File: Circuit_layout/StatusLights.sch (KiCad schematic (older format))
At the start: 34 parts, among them Q1 ZVP4525G, U1 PDM2-S24-S12, U11 TLP293, U12 TLP293, U16 LTC3638, U27 TLP293

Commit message: Completed errata changes
Committing before annotation, footprint assignment, and board relayout for backup purposes
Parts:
- removed C19: 10uF, Capacitors_SMD:C_0805_HandSoldering, symbol C
- removed C3: 2.2uF, Capacitors_SMD:C_0805_HandSoldering, symbol C
- removed D5: D_Schottky, custom_footprints:do214ac, symbol D_Schottky
- removed L1: 100uH, Inductors:Inductor_Taiyo-Yuden_NR-80xx_HandSoldering, symbol INDUCTOR
- removed R16, R19, R20, R69: 250k, Resistors_SMD:R_0805_HandSoldering, symbol R
- removed R70: 47k, Resistors_SMD:R_0805_HandSoldering, symbol R
- removed R76: 750k, Resistors_SMD:R_0805_HandSoldering, symbol R
- removed R77: 196k, Resistors_SMD:R_0805_HandSoldering, symbol R
- removed U1: PDM2-S24-S12, custom_footprints:DCDC-Conv_TRACO_TMR_1-xxxx_Single, symbol PDM2-S24-S12-RESCUE-Circuit_layout
- removed U16: LTC3638, custom_footprints:TSSOP16_LTC3638, symbol LTC3638
- added R?: 4.3K, symbol R
- added R?: 250k, symbol R
- added U?: RUW15SL12C, symbol RUW15SL12C
- C?: renamed from C24; value 1uF -> 10uF
- D1, D2, D3, D4: symbol LED -> LED-RESCUE-Circuit_layout
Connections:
- net GND: now also U?.8 (-Vout)
- net HV+: now also HVPL_HV1.1, R?.2, U?.5 (+Vin)
- net HV-: now also R?.2, U?.4 (-Vin)
- net HVPL: now also U?.7 (+Vout)
- new net: R?.1, R?.1, U?.1 (ON/OFF)
- no-connect marks 1 -> 3
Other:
- moved on the sheet: C?, GLV_GND1, HVPL_HV1, HVPL_LV1, HV_GND1

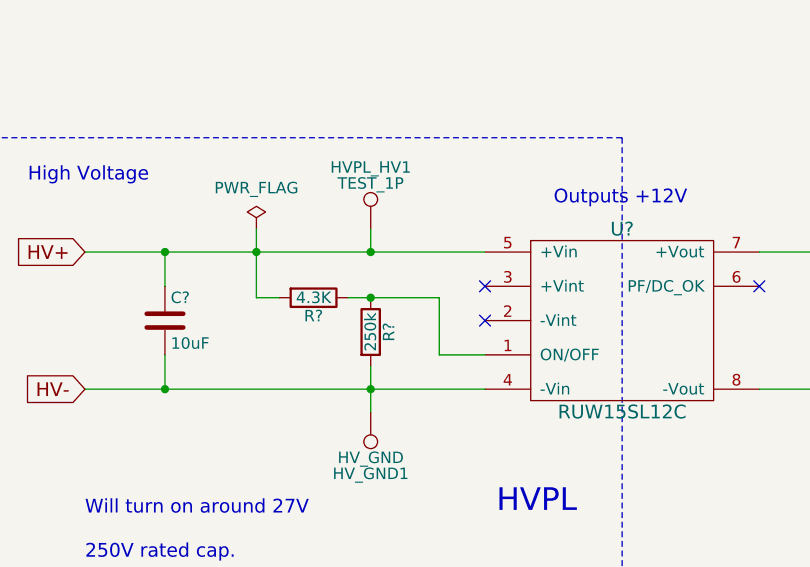
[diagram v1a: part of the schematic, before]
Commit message: Associated footprints and generated new netlist
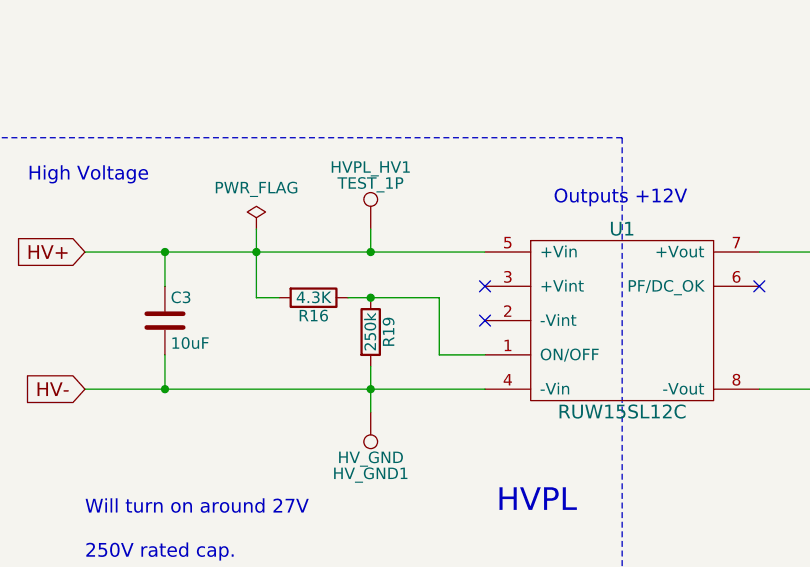
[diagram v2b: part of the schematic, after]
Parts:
- C3: renamed from C?; footprint Capacitors_SMD:C_2220_HandSoldering -> Capacitors_THT:CP_Radial_D10.0mm_P5.00mm
- R16, R19: renamed from R?; footprint (none) -> Resistors_SMD:R_0805_HandSoldering
- U1: renamed from U?; footprint (none) -> custom_footprints:RUW15
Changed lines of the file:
@@
 $EndComp
 $Comp
-L C C?
+L C C3
 U 1 1 58C1AF35
 P 1200 5600
-F 0 "C?" H 1225 5700 50  0000 L CNN
+F 0 "C3" H 1225 5700 50  0000 L CNN
 F 1 "10uF" H 1225 5500 50  0000 L CNN
-F 2 "Capacitors_SMD:C_2220_HandSoldering" H 1238 5450 50  0001 C CNN
+F 2 "Capacitors_THT:CP_Radial_D10.0mm_P5.00mm" H 1238 5450 50  0001 C CNN
 F 3 "" H 1200 5600 50  0000 C CNN
 F 4 "490-3550-1-ND" H 1200 5600 60  0001 C CNN "DigiKey P/N"
@@
 NoConn ~ 2600 5450
 $Comp
-L RUW15SL12C U?
+L RUW15SL12C U1
 U 1 1 5A7E5026
 P 3200 5600
-F 0 "U?" H 3200 6000 60  0000 C CNN
+F 0 "U1" H 3200 6000 60  0000 C CNN
 F 1 "RUW15SL12C" H 3200 5200 60  0000 C CNN
-F 2 "" H 2850 6000 60  0001 C CNN
+F 2 "custom_footprints:RUW15" H 2850 6000 60  0001 C CNN
 F 3 "" H 2850 6000 60  0001 C CNN
 	1    3200 5600
@@
 NoConn ~ 3800 5450
 $Comp
-L R R?
+L R R16
 U 1 1 5A7E9A17
 P 1850 5500
-F 0 "R?" V 1930 5500 50  0000 C CNN
+F 0 "R16" V 1930 5500 50  0000 C CNN
 F 1 "4.3K" V 1850 5500 50  0000 C CNN
-F 2 "" V 1780 5500 50  0000 C CNN
+F 2 "Resistors_SMD:R_0805_HandSoldering" V 1780 5500 50  0001 C CNN
 F 3 "" H 1850 5500 50  0000 C CNN
 	1    1850 5500
@@
 $EndComp
 $Comp
-L R R?
+L R R19
 U 1 1 5A7E9ABB
 P 2100 5650
-F 0 "R?" V 2180 5650 50  0000 C CNN
+F 0 "R19" V 2180 5650 50  0000 C CNN
 F 1 "250k" V 2100 5650 50  0000 C CNN
-F 2 "" V 2030 5650 50  0000 C CNN
+F 2 "Resistors_SMD:R_0805_HandSoldering" V 2030 5650 50  0001 C CNN
 F 3 "" H 2100 5650 50  0000 C CNN
 	1    2100 5650

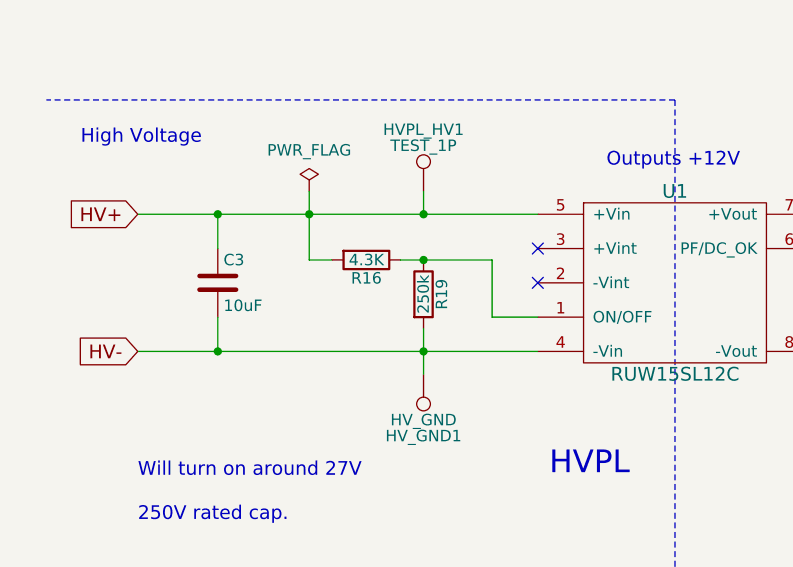
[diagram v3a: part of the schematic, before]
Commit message: Wider traces for DC/DC converter
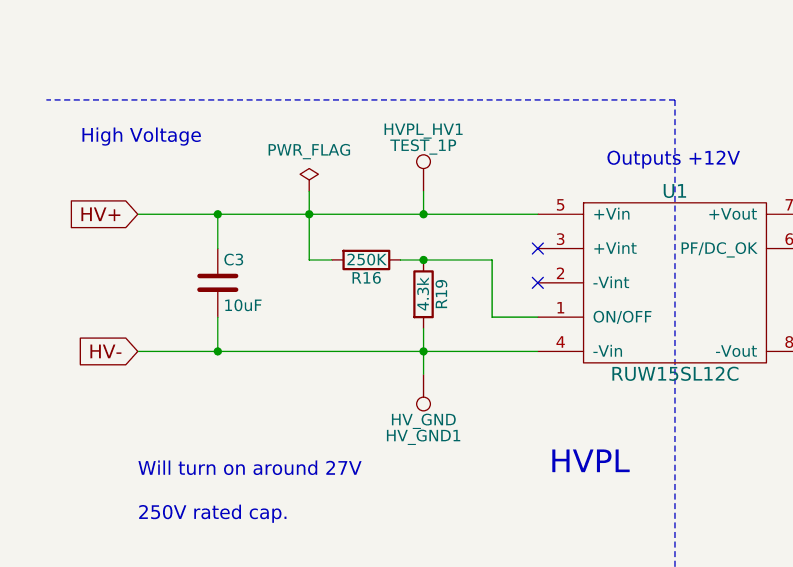
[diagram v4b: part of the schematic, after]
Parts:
- R16: value 4.3K -> 250K
- R19: value 250k -> 4.3k
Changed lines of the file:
@@
 P 1850 5500
 F 0 "R16" V 1930 5500 50  0000 C CNN
-F 1 "4.3K" V 1850 5500 50  0000 C CNN
+F 1 "250K" V 1850 5500 50  0000 C CNN
 F 2 "Resistors_SMD:R_0805_HandSoldering" V 1780 5500 50  0001 C CNN
 F 3 "" H 1850 5500 50  0000 C CNN
@@
 P 2100 5650
 F 0 "R19" V 2180 5650 50  0000 C CNN
-F 1 "250k" V 2100 5650 50  0000 C CNN
+F 1 "4.3k" V 2100 5650 50  0000 C CNN
 F 2 "Resistors_SMD:R_0805_HandSoldering" V 2030 5650 50  0001 C CNN
 F 3 "" H 2100 5650 50  0000 C CNN

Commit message: Generated gerber and drill files for board ordering
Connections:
- net CC_LED renamed SPARE_LED
- net CC_LED_CTRL renamed SPARE_LED_CTRL
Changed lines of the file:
@@
 $EndComp
 $Comp
-L GND #PWR038
+L GND #PWR043
 U 1 1 58AF33D9
 P 4250 1300
-F 0 "#PWR038" H 4250 1050 50  0001 C CNN
+F 0 "#PWR043" H 4250 1050 50  0001 C CNN
 F 1 "GND" H 4250 1150 50  0000 C CNN
 F 2 "" H 4250 1300 50  0000 C CNN
@@
 $EndComp
 $Comp
-L +24V #PWR039
+L +24V #PWR044
 U 1 1 58AF3526
 P 5650 850
-F 0 "#PWR039" H 5650 700 50  0001 C CNN
+F 0 "#PWR044" H 5650 700 50  0001 C CNN
 F 1 "+24V" H 5650 990 50  0000 C CNN
 F 2 "" H 5650 850 50  0000 C CNN
@@
 $EndComp
 $Comp
-L GND #PWR040
+L GND #PWR045
 U 1 1 58AF4273
 P 4250 2500
-F 0 "#PWR040" H 4250 2250 50  0001 C CNN
+F 0 "#PWR045" H 4250 2250 50  0001 C CNN
 F 1 "GND" H 4250 2350 50  0000 C CNN
 F 2 "" H 4250 2500 50  0000 C CNN
@@
 $EndComp
 $Comp
-L +24V #PWR041
+L +24V #PWR046
 U 1 1 58AF427B
 P 5650 2000
-F 0 "#PWR041" H 5650 1850 50  0001 C CNN
+F 0 "#PWR046" H 5650 1850 50  0001 C CNN
 F 1 "+24V" H 5650 2140 50  0000 C CNN
 F 2 "" H 5650 2000 50  0000 C CNN
@@
 $EndComp
 $Comp
-L GND #PWR042
+L GND #PWR047
 U 1 1 58B26825
 P 8750 1200
-F 0 "#PWR042" H 8750 950 50  0001 C CNN
+F 0 "#PWR047" H 8750 950 50  0001 C CNN
 F 1 "GND" H 8750 1050 50  0000 C CNN
 F 2 "" H 8750 1200 50  0000 C CNN
@@
 $EndComp
 $Comp
-L GND #PWR043
+L GND #PWR048
 U 1 1 58B26F4E
 P 8750 1650
-F 0 "#PWR043" H 8750 1400 50  0001 C CNN
+F 0 "#PWR048" H 8750 1400 50  0001 C CNN
 F 1 "GND" H 8750 1500 50  0000 C CNN
 F 2 "" H 8750 1650 50  0000 C CNN
@@
 $EndComp
 $Comp
-L GND #PWR044
+L GND #PWR049
 U 1 1 58B272AA
 P 8750 2100
-F 0 "#PWR044" H 8750 1850 50  0001 C CNN
+F 0 "#PWR049" H 8750 1850 50  0001 C CNN
 F 1 "GND" H 8750 1950 50  0000 C CNN
 F 2 "" H 8750 2100 50  0000 C CNN
@@
 $EndComp
 $Comp
-L GND #PWR045
+L GND #PWR050
 U 1 1 58B27330
 P 8750 2550
-F 0 "#PWR045" H 8750 2300 50  0001 C CNN
+F 0 "#PWR050" H 8750 2300 50  0001 C CNN
 F 1 "GND" H 8750 2400 50  0000 C CNN
 F 2 "" H 8750 2550 50  0000 C CNN
@@
 Blue
 $Comp
-L +5V #PWR046
+L +5V #PWR051
 U 1 1 58B2809B
 P 10250 1100
-F 0 "#PWR046" H 10250 950 50  0001 C CNN
+F 0 "#PWR051" H 10250 950 50  0001 C CNN
 F 1 "+5V" H 10250 1240 50  0000 C CNN
 F 2 "" H 10250 1100 50  0000 C CNN
@@
 	4800 4500 4950 4500
 $Comp
-L +24V #PWR047
+L +24V #PWR052
 U 1 1 58C523A5
 P 4800 3700
-F 0 "#PWR047" H 4800 3550 50  0001 C CNN
+F 0 "#PWR052" H 4800 3550 50  0001 C CNN
 F 1 "+24V" H 4800 3840 50  0000 C CNN
 F 2 "" H 4800 3700 50  0000 C CNN
@@
 $EndComp
 $Comp
-L PWR_FLAG #FLG048
+L PWR_FLAG #FLG053
 U 1 1 58C1AF3D
 P 1600 5200
-F 0 "#FLG048" H 1600 5295 50  0001 C CNN
+F 0 "#FLG053" H 1600 5295 50  0001 C CNN
 F 1 "PWR_FLAG" H 1600 5380 50  0000 C CNN
 F 2 "" H 1600 5200 50  0000 C CNN
@@
 	1250 1600 1400 1600
 $Comp
-L GND #PWR049
+L GND #PWR054
 U 1 1 58D3C796
 P 4700 6000
-F 0 "#PWR049" H 4700 5750 50  0001 C CNN
+F 0 "#PWR054" H 4700 5750 50  0001 C CNN
 F 1 "GND" H 4700 5850 50  0000 C CNN
 F 2 "" H 4700 6000 50  0000 C CNN
@@
 HV-
 Text HLabel 1250 2050 0    60   Input ~ 0
-CC_LED_CTRL
+SPARE_LED_CTRL
 Text Label 1400 2050 0    60   ~ 0
-CC_LED_CTRL
+SPARE_LED_CTRL
 Wire Wire Line
 	1250 2050 1400 2050
@@
 $EndComp
 $Comp
-L GND #PWR050
+L GND #PWR055
 U 1 1 58DA1E52
 P 4250 3350
-F 0 "#PWR050" H 4250 3100 50  0001 C CNN
+F 0 "#PWR055" H 4250 3100 50  0001 C CNN
 F 1 "GND" H 4250 3200 50  0000 C CNN
 F 2 "" H 4250 3350 50  0000 C CNN
@@
 $EndComp
 $Comp
-L +24V #PWR051
+L +24V #PWR056
 U 1 1 58DA1E58
 P 5650 2850
-F 0 "#PWR051" H 5650 2700 50  0001 C CNN
+F 0 "#PWR056" H 5650 2700 50  0001 C CNN
 F 1 "+24V" H 5650 2990 50  0000 C CNN
 F 2 "" H 5650 2850 50  0000 C CNN
@@
 $EndComp
 Text Label 5400 3200 0    60   ~ 0
-CC_LED
-Text Label 3250 3000 0    60   ~ 0
-CC_LED_CTRL
+SPARE_LED
+Text Label 2950 3000 0    60   ~ 0
+SPARE_LED_CTRL
 Wire Wire Line
 	4250 3200 4300 3200
@@
 	4900 3200 5400 3200
 Wire Wire Line
-	3750 3000 3250 3000
+	2950 3000 3750 3000
 Wire Wire Line
 	5650 3000 5650 2850
 Text GLabel 1250 1000 0    60   Input ~ 0
-CC_LED
+SPARE_LED
 Text Label 1400 1000 0    60   ~ 0
-CC_LED
+SPARE_LED
 Wire Wire Line
 	1250 1000 1400 1000

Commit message: Schematic update
Changed schematic to reflect board as assembeled
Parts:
- removed R16: 250K, Resistors_SMD:R_0805_HandSoldering, symbol R
- removed R19: 4.3k, Resistors_SMD:R_0805_HandSoldering, symbol R
- added R?: 200R/2W, Resistors_SMD:R_0805_HandSoldering, symbol R
- C3: footprint Capacitors_THT:CP_Radial_D10.0mm_P5.00mm -> Capacitors_SMD:CP_Elec_8x10
- HVPL_LV1: value HVPL_LV -> TSAL_LV
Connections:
- net GND: now also R?.1
- net HVPL renamed TSAL
- net TSAL: now also R?.2
- no-connect marks 3 -> 4
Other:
- note added: "Pins 6 and 8 are reversed on the footprint\nFootpirnt and layout need to be fixed"
- note added: "R16 and R19 removed\non current board"
- note added: "Resistor added for loading DC/DC\nconverter to minimum current (.125A)\nShould be 96R/2W"
- note added: "TSAL"
- note added: "Will turn on around 16V\n\n250V rated cap."
- note removed: "HVPL"
- note removed: "Will turn on around 27V\n\n250V rated cap."
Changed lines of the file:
@@
 LIBS:ftdi
 LIBS:gennum
-LIBS:graphic
 LIBS:hc11
 LIBS:intel
@@
 LIBS:Lattice
 LIBS:linear
-LIBS:logo
 LIBS:maxim
 LIBS:memory
@@
 F 0 "C3" H 1225 5700 50  0000 L CNN
 F 1 "10uF" H 1225 5500 50  0000 L CNN
-F 2 "Capacitors_THT:CP_Radial_D10.0mm_P5.00mm" H 1238 5450 50  0001 C CNN
+F 2 "Capacitors_SMD:CP_Elec_8x10" H 1238 5450 50  0001 C CNN
 F 3 "" H 1200 5600 50  0000 C CNN
 F 4 "490-3550-1-ND" H 1200 5600 60  0001 C CNN "DigiKey P/N"
@@
 	1    0    0    -1
 $EndComp
-Wire Wire Line
-	1600 5200 1600 5500
-Connection ~ 1600 5300
 Connection ~ 1200 5300
 $Comp
@@
 $EndComp
 Text GLabel 1250 1600 0    60   Input ~ 0
-HVPL
+TSAL
 Text Label 1400 1600 0    60   ~ 0
-HVPL
+TSAL
 Wire Wire Line
 	1250 1600 1400 1600
@@
 $EndComp
 Text Label 5000 5300 2    60   ~ 0
-HVPL
-Text Notes 5050 5700 0    60   ~ 0
+TSAL
+Text Notes 4800 5150 0    60   ~ 0
 Note: this is going to three LEDs
 Text Notes 2900 5100 0    60   ~ 0
@@
 P 4300 5200
 F 0 "HVPL_LV1" H 4300 5470 50  0000 C CNN
-F 1 "HVPL_LV" H 4300 5400 50  0000 C CNN
+F 1 "TSAL_LV" H 4300 5400 50  0000 C CNN
 F 2 "Measurement_Points:Measurement_Point_Round-SMD-Pad_Big" H 4500 5200 50  0001 C CNN
 F 3 "" H 4500 5200 50  0000 C CNN
@@
 $EndComp
 Wire Wire Line
-	4300 6000 4300 5900
+	4300 5750 4300 6000
 Connection ~ 4300 5900
 Wire Wire Line
-	4300 5200 4300 5300
+	4300 5200 4300 5450
 Connection ~ 4300 5300
 $Comp
@@
 	1    0    0    -1
 $EndComp
-Wire Wire Line
-	2100 5800 2100 6000
 Connection ~ 2100 5900
 Wire Wire Line
@@
 	1250 1000 1400 1000
 Text Notes 2650 6450 0    99   ~ 0
-HVPL
+TSAL
 NoConn ~ 2600 5450
 $Comp
@@
 	3800 5300 5000 5300
 NoConn ~ 3800 5450
-$Comp
-L R R16
-U 1 1 5A7E9A17
-P 1850 5500
-F 0 "R16" V 1930 5500 50  0000 C CNN
-F 1 "250K" V 1850 5500 50  0000 C CNN
-F 2 "Resistors_SMD:R_0805_HandSoldering" V 1780 5500 50  0001 C CNN
-F 3 "" H 1850 5500 50  0000 C CNN
-	1    1850 5500
-	0    1    1    0
-$EndComp
-$Comp
-L R R19
-U 1 1 5A7E9ABB
-P 2100 5650
-F 0 "R19" V 2180 5650 50  0000 C CNN
-F 1 "4.3k" V 2100 5650 50  0000 C CNN
-F 2 "Resistors_SMD:R_0805_HandSoldering" V 2030 5650 50  0001 C CNN
-F 3 "" H 2100 5650 50  0000 C CNN
-	1    2100 5650
-	1    0    0    -1
-$EndComp
-Wire Wire Line
-	1600 5500 1700 5500
-Wire Wire Line
-	2000 5500 2400 5500
-Wire Wire Line
-	2400 5500 2400 5750
-Wire Wire Line
-	2400 5750 2600 5750
-Connection ~ 2100 5500
 Text Notes 850  6650 0    60   ~ 0
-Will turn on around 27V\n\n250V rated cap.
+Will turn on around 16V\n\n250V rated cap.
+Wire Wire Line
+	1600 5200 1600 5300
+Connection ~ 1600 5300
+NoConn ~ 2600 5750
+Wire Wire Line
+	2100 5900 2100 6000
+Text Notes 1500 5650 0    60   ~ 0
+R16 and R19 removed\non current board
+$Comp
+L R R?
+U 1 1 5ACB41D1
+P 4300 5600
+F 0 "R?" V 4380 5600 50  0000 C CNN
+F 1 "200R/2W" V 4300 5600 50  0000 C CNN
+F 2 "Resistors_SMD:R_0805_HandSoldering" V 4230 5600 50  0001 C CNN
+F 3 "" H 4300 5600 50  0000 C CNN
+F 4 "P10.0KCCT-ND" V 4300 5600 60  0001 C CNN "DigiKey P/N"
+F 5 "http://www.digikey.com/product-detail/en/panasonic-electronic-components/ERJ-6ENF1002V/P10.0KCCT-ND/119248" V 4300 5600 60  0001 C CNN "URL"
+F 6 "ERJ-6ENF1002V" V 4300 5600 60  0001 C CNN "Man P/N"
+	1    4300 5600
+	-1   0    0    1
+$EndComp
+Text Notes 4400 5800 0    60   ~ 0
+Resistor added for loading DC/DC\nconverter to minimum current (.125A)\nShould be 96R/2W
+Text Notes 3300 6500 0    60   ~ 0
+Pins 6 and 8 are reversed on the footprint\nFootpirnt and layout need to be fixed
 $EndSCHEMATC
